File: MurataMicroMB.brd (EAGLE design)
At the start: 90 x 63 mm, 54 parts, among them CON1 C-2395, CON2 WM17143CT-ND, CON3 CON_MIL_10_ARM, CON4 C-2395, IC1 NC7SZ00M5XCT-ND, IC2 296-35164-1-ND, IC3 IC_LPC11U3XQFN33, IC4 AZ1117EH-3.3TRG1DICT-ND, Q1 1253-1168-1-ND, SW1 P-8073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

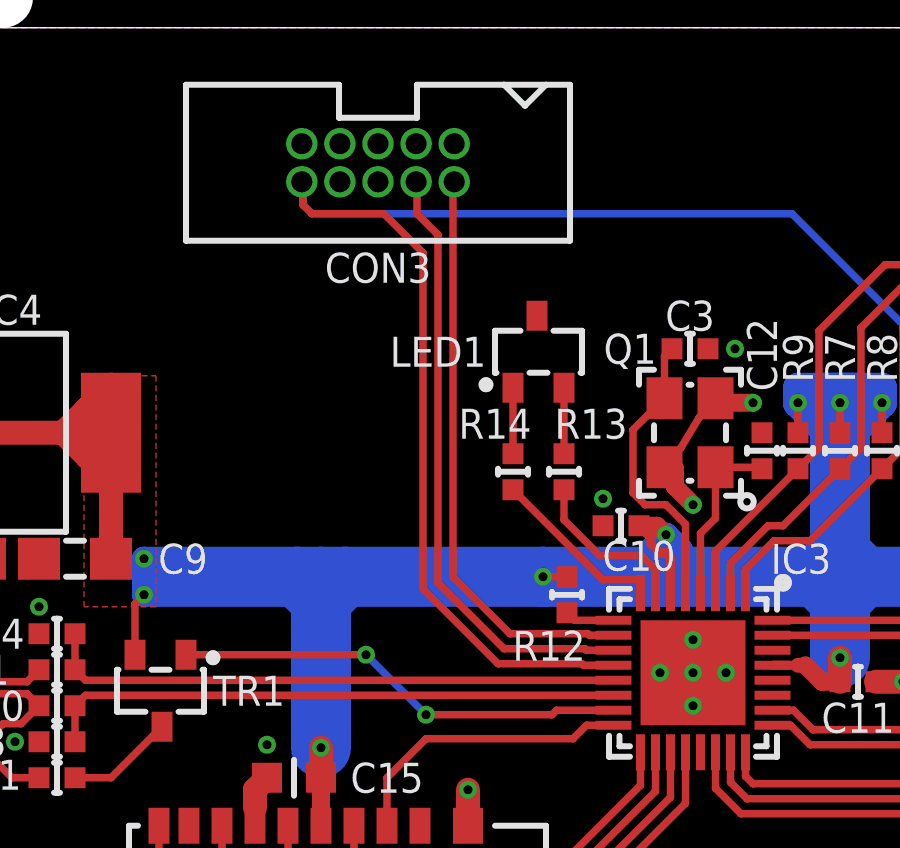
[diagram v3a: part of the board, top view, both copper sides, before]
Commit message: [ MB ] add R17-19
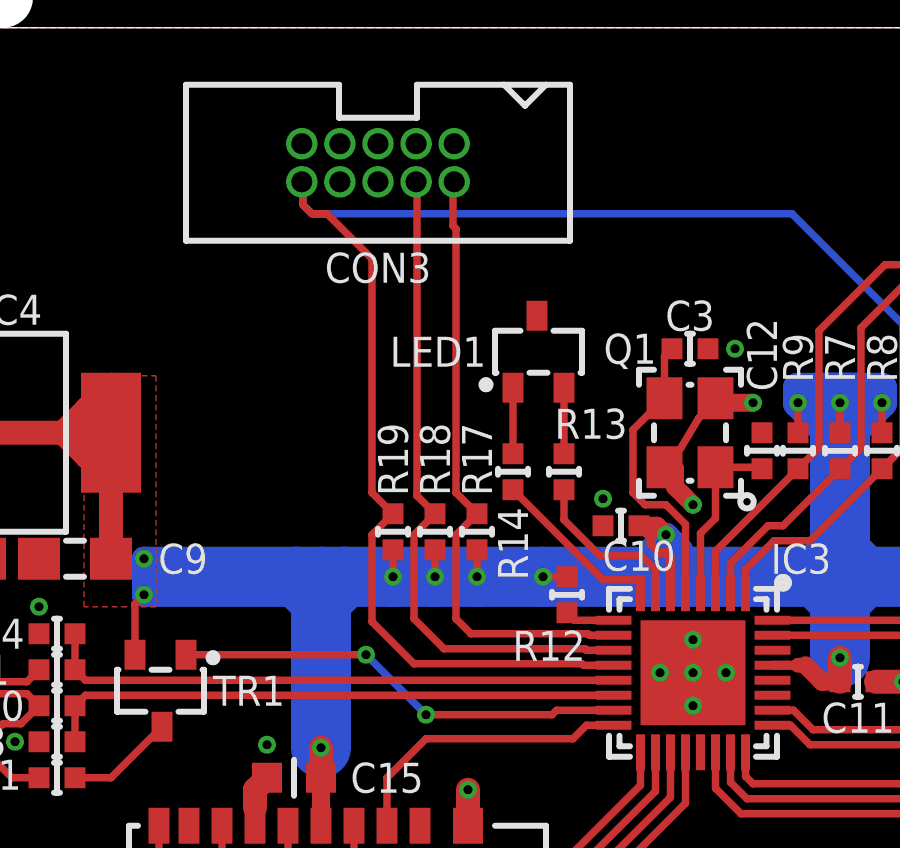
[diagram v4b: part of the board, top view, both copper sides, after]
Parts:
- added R17, R18, R19: 10k/1005, mylib:C0402
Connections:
- net 3.3V: now also R17.2, R18.2, R19.2
- net NSRST: now also R19.1
- net SWCLK: now also R18.1
- net SWDIO: now also R17.1
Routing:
- net 3.3V: track 131.2 -> 133.9 mm, vias 11 -> 14
- net SWCLK: track 20.4 -> 22.2 mm
- net SWDIO: track 19.4 -> 20.7 mm
- net NSRST: track 59.9 -> 61.0 mm
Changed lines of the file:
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@@
 </element>
 <element name="R14" library="mylib" package="C0402" value="100/1005" x="36" y="38.2" smashed="yes" rot="R90">
-<attribute name="NAME" x="35.4" y="39.8" size="1" layer="25" font="vector" ratio="20" rot="R180" align="center"/>
+<attribute name="NAME" x="36" y="35.8" size="1" layer="25" font="vector" ratio="20" rot="R270" align="center"/>
 <attribute name="VALUE" x="37.9" y="37.6" size="1" layer="27" font="vector" ratio="20" rot="R90"/>
 </element>
@@
 <attribute name="MF" value="" x="62.4" y="18.7" size="1.2" layer="27" ratio="17" rot="R180" display="off"/>
 <attribute name="OC_FARNELL" value="unknown" x="62.4" y="18.7" size="1.2" layer="27" ratio="17" rot="R180" display="off"/>
+</element>
+<element name="R17" library="mylib" package="C0402" value="10k/1005" x="34.8" y="36.2" smashed="yes" rot="R270">
+<attribute name="NAME" x="35.3" y="37.4" size="1" layer="25" font="vector" ratio="20" rot="R90"/>
+<attribute name="VALUE" x="32.9" y="36.8" size="1" layer="27" font="vector" ratio="20" rot="R270"/>
+</element>
+<element name="R18" library="mylib" package="C0402" value="10k/1005" x="33.4" y="36.2" smashed="yes" rot="R270">
+<attribute name="NAME" x="33.9" y="37.4" size="1" layer="25" font="vector" ratio="20" rot="R90"/>
+<attribute name="VALUE" x="31.5" y="36.8" size="1" layer="27" font="vector" ratio="20" rot="R270"/>
+</element>
+<element name="R19" library="mylib" package="C0402" value="10k/1005" x="32" y="36.2" smashed="yes" rot="R270">
+<attribute name="NAME" x="32.5" y="37.4" size="1" layer="25" font="vector" ratio="20" rot="R90"/>
+<attribute name="VALUE" x="30.1" y="36.8" size="1" layer="27" font="vector" ratio="20" rot="R270"/>
 </element>
 </elements>
@@
 <wire x1="32.77" y1="47.865" x2="32.77" y2="47.83" width="0.25" layer="1"/>
 <wire x1="32.77" y1="47.83" x2="32.8" y2="47.8" width="0.25" layer="1"/>
-<wire x1="32.8" y1="47.8" x2="32.8" y2="46.8" width="0.25" layer="1"/>
-<wire x1="32.8" y1="46.8" x2="33.5" y2="46.1" width="0.25" layer="1"/>
-<wire x1="33.5" y1="46.1" x2="33.5" y2="34.5" width="0.25" layer="1"/>
-<wire x1="33.5" y1="34.5" x2="35.7" y2="32.3" width="0.25" layer="1"/>
-<wire x1="35.7" y1="32.3" x2="38.4" y2="32.3" width="0.25" layer="1"/>
+<wire x1="32.7" y1="33.3" x2="33.7" y2="32.3" width="0.25" layer="1"/>
+<wire x1="33.7" y1="32.3" x2="38.4" y2="32.3" width="0.25" layer="1"/>
+<wire x1="32.8" y1="47.8" x2="32.8" y2="37.4" width="0.25" layer="1"/>
+<contactref element="R18" pad="1"/>
+<wire x1="32.7" y1="36.1" x2="32.7" y2="33.3" width="0.25" layer="1"/>
+<wire x1="33.4" y1="36.8" x2="32.7" y2="36.1" width="0.25" layer="1"/>
+<wire x1="32.8" y1="37.4" x2="33.4" y2="36.8" width="0.25" layer="1"/>
 </signal>
 <signal name="SWDIO">
@@
 <wire x1="34.1" y1="47.805" x2="34.1" y2="47.8" width="0.25" layer="1"/>
 <wire x1="34.1" y1="47.8" x2="34" y2="47.7" width="0.25" layer="1"/>
-<wire x1="34" y1="47.7" x2="34" y2="34.7" width="0.25" layer="1"/>
-<wire x1="34" y1="34.7" x2="35.9" y2="32.8" width="0.25" layer="1"/>
-<wire x1="35.9" y1="32.8" x2="38.5" y2="32.8" width="0.25" layer="1"/>
+<wire x1="34" y1="47.7" x2="34" y2="46.4" width="0.25" layer="1"/>
+<wire x1="34" y1="46.4" x2="34.1" y2="46.3" width="0.25" layer="1"/>
+<wire x1="34.1" y1="46.3" x2="34.1" y2="37.5" width="0.25" layer="1"/>
+<wire x1="34.1" y1="36.1" x2="34.1" y2="33.3" width="0.25" layer="1"/>
+<wire x1="34.1" y1="33.3" x2="34.6" y2="32.8" width="0.25" layer="1"/>
+<wire x1="34.6" y1="32.8" x2="38.5" y2="32.8" width="0.25" layer="1"/>
+<contactref element="R17" pad="1"/>
+<wire x1="34.8" y1="36.8" x2="34.1" y2="36.1" width="0.25" layer="1"/>
+<wire x1="34.1" y1="37.5" x2="34.8" y2="36.8" width="0.25" layer="1"/>
 </signal>
 <signal name="NSRST">
@@
 <wire x1="39.35" y1="31.75" x2="38.35" y2="31.75" width="0.25" layer="1"/>
 <wire x1="38.35" y1="31.75" x2="38.3" y2="31.8" width="0.25" layer="1"/>
-<wire x1="35.5" y1="31.8" x2="38.3" y2="31.8" width="0.25" layer="1"/>
+<wire x1="32.7" y1="31.8" x2="38.3" y2="31.8" width="0.25" layer="1"/>
 <wire x1="29" y1="47.825" x2="29" y2="47.8" width="0.25" layer="1"/>
 <wire x1="29" y1="47.8" x2="28.9" y2="47.7" width="0.25" layer="1"/>
@@
 <wire x1="29.3" y1="46.8" x2="29" y2="47.1" width="0.25" layer="16"/>
 <wire x1="29" y1="47.825" x2="28.96" y2="47.865" width="0.25" layer="1"/>
-<wire x1="35.5" y1="31.8" x2="33" y2="34.3" width="0.25" layer="1"/>
-<wire x1="33" y1="34.3" x2="33" y2="45.5" width="0.25" layer="1"/>
+<wire x1="32.7" y1="31.8" x2="31.3" y2="33.2" width="0.25" layer="1"/>
+<wire x1="31.3" y1="33.2" x2="31.3" y2="36.1" width="0.25" layer="1"/>
+<wire x1="31.3" y1="37.5" x2="31.3" y2="45.3" width="0.25" layer="1"/>
 <wire x1="29" y1="47.6" x2="29" y2="47.1" width="0.25" layer="1"/>
-<wire x1="33" y1="45.5" x2="31.7" y2="46.8" width="0.25" layer="1"/>
-<wire x1="31.7" y1="46.8" x2="29.3" y2="46.8" width="0.25" layer="1"/>
+<wire x1="31.3" y1="45.3" x2="29.8" y2="46.8" width="0.25" layer="1"/>
+<wire x1="29.8" y1="46.8" x2="29.3" y2="46.8" width="0.25" layer="1"/>
 <wire x1="29.3" y1="46.8" x2="29" y2="47.1" width="0.25" layer="1"/>
+<contactref element="R19" pad="1"/>
+<wire x1="32" y1="36.8" x2="31.3" y2="36.1" width="0.25" layer="1"/>
+<wire x1="31.3" y1="37.5" x2="32" y2="36.8" width="0.25" layer="1"/>
 </signal>
 <signal name="3.3V">
@@
 <wire x1="28.8" y1="34.7" x2="29.6" y2="34.7" width="2" layer="16"/>
 <wire x1="29.6" y1="34.7" x2="30.4" y2="34.7" width="2" layer="16"/>
-<wire x1="30.4" y1="34.7" x2="37" y2="34.7" width="2" layer="16"/>
+<wire x1="30.4" y1="34.7" x2="32" y2="34.7" width="2" layer="16"/>
+<wire x1="32" y1="34.7" x2="33.4" y2="34.7" width="2" layer="16"/>
+<wire x1="33.4" y1="34.7" x2="34.8" y2="34.7" width="2" layer="16"/>
+<wire x1="34.8" y1="34.7" x2="37" y2="34.7" width="2" layer="16"/>
 <wire x1="37" y1="34.7" x2="41.1" y2="34.7" width="2" layer="16"/>
 <wire x1="23.7" y1="35.3" x2="24.4" y2="34.7" width="0.8" layer="16"/>
@@
 <wire x1="44.65" y1="31.75" x2="45.5" y2="31.75" width="0.3" layer="1"/>
 <wire x1="46.9" y1="32" x2="46.9" y2="31.2" width="0.8" layer="1"/>
+<contactref element="R17" pad="2"/>
+<contactref element="R18" pad="2"/>
+<contactref element="R19" pad="2"/>
+<via x="32" y="34.7" extent="1-16" drill="0.3"/>
+<via x="33.4" y="34.7" extent="1-16" drill="0.3"/>
+<via x="34.8" y="34.7" extent="1-16" drill="0.3"/>
+<wire x1="32" y1="35.6" x2="32" y2="34.7" width="0.25" layer="1"/>
+<wire x1="33.4" y1="35.6" x2="33.4" y2="34.7" width="0.25" layer="1"/>
+<wire x1="34.8" y1="35.6" x2="34.8" y2="34.7" width="0.25" layer="1"/>
 </signal>
 <signal name="N$3">

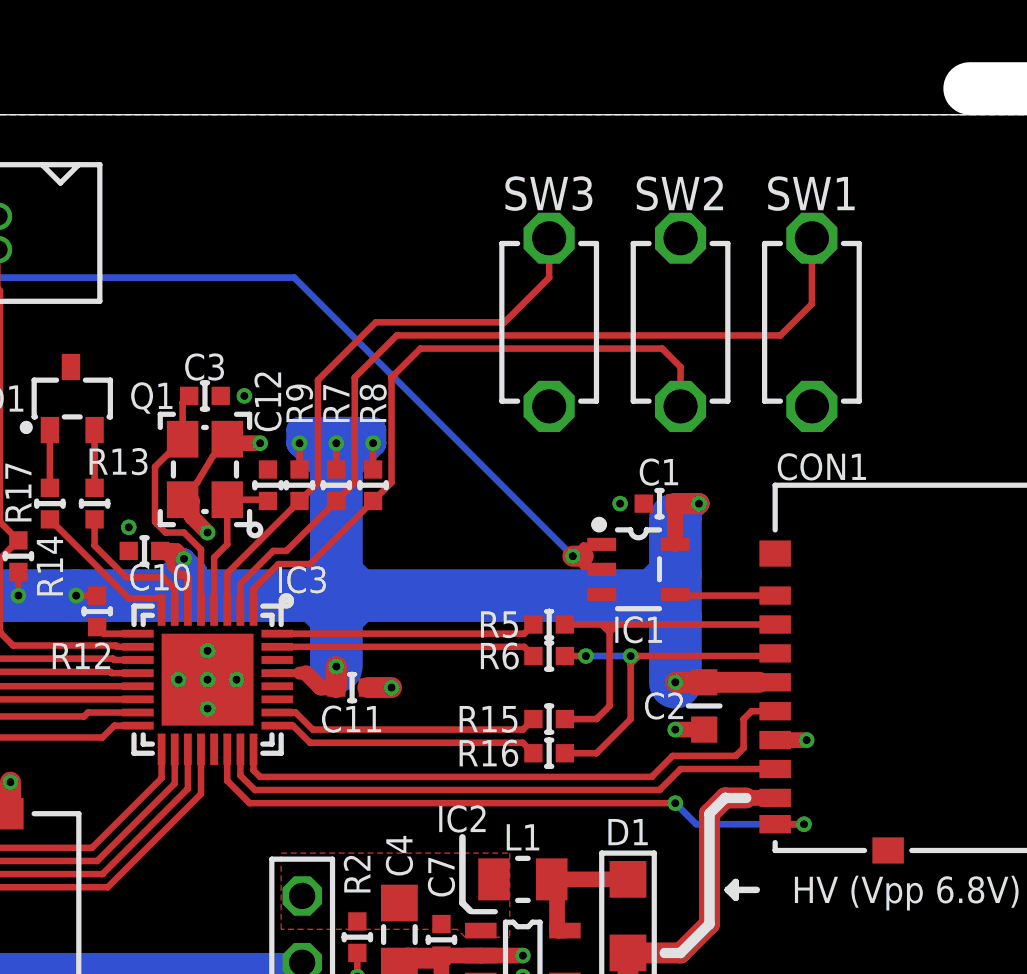
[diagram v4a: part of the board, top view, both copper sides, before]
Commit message: [ MB ] add R20/21; R7/8/9 move
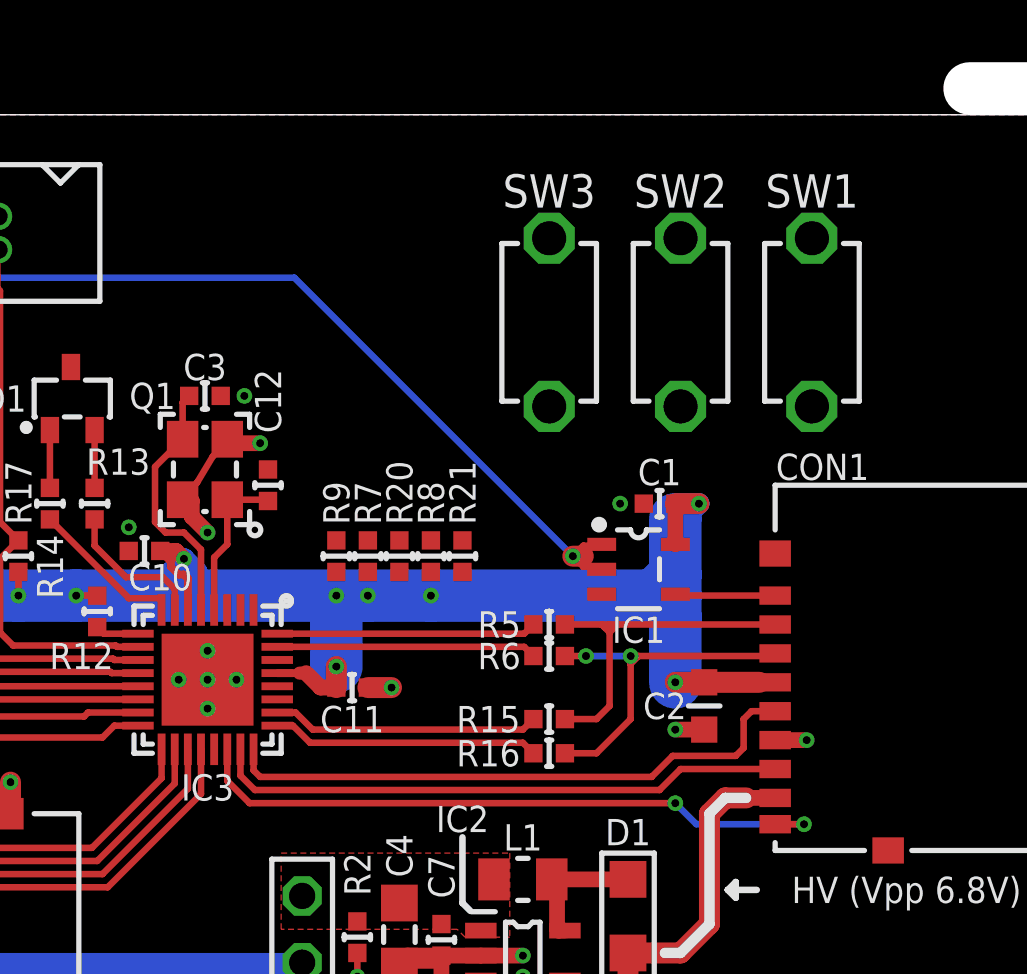
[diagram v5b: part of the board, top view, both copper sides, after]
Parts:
- added R20, R21: 1k/1005, mylib:C0402
- R15, R16, R5, R6: value 33/1005 -> 1k/1005
- moved R8 3.48 mm to (50.5, 36.2), turned to 90 degrees
- moved R9 3.04 mm to (46.9, 36.2), turned to 90 degrees
- moved R7 2.95 mm to (48.1, 36.2), turned to 90 degrees
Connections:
- new net N$19: R21.1, SW2.A2
- new net N$21: IC3.1, R20.2
- net BL: now also R20.1, R21.2; no longer IC3.1, SW2.A2
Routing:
- net !RESET!: track 32.0 -> 0.00 mm
- net 3.3V: track 133.9 -> 108.0 mm
- net BL: track 25.0 -> 0.00 mm
- net ISP: track 22.1 -> 0.00 mm

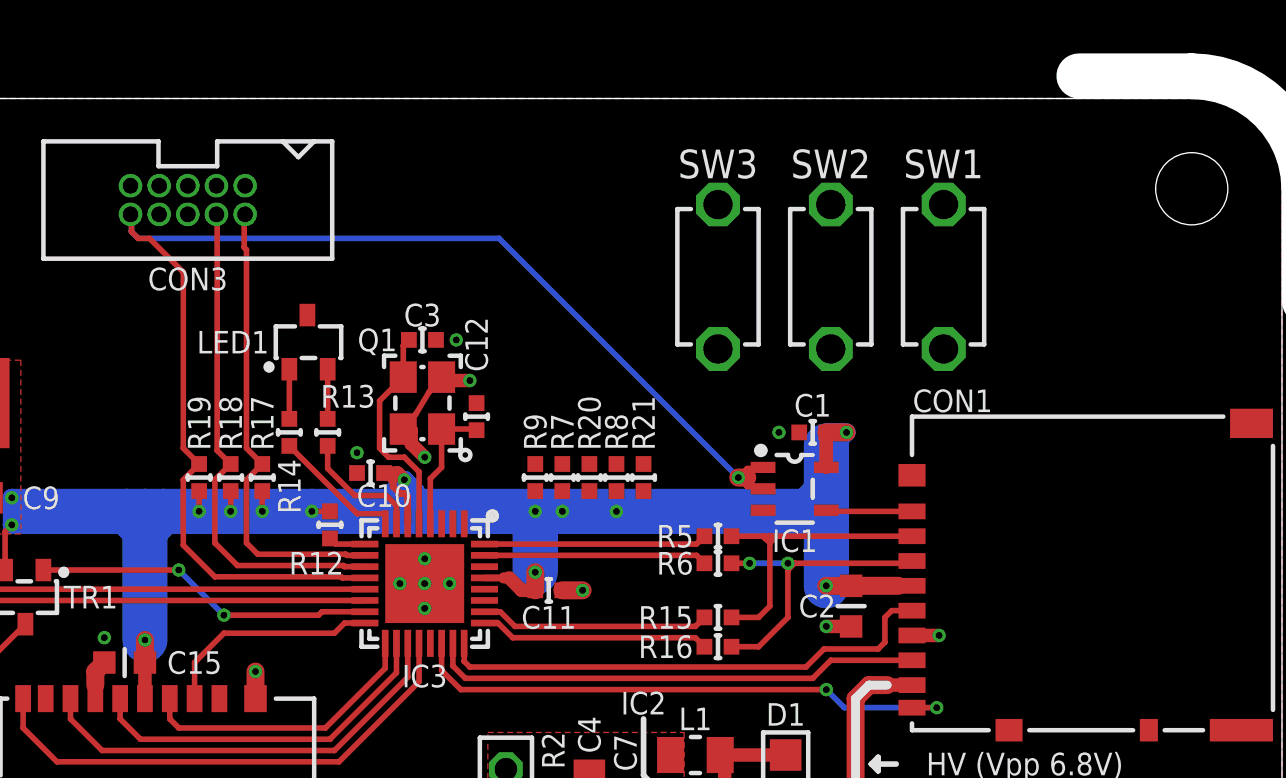
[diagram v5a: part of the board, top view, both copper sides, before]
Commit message: [ MB ] move SW1-3, BL shares IC1 with nSRST
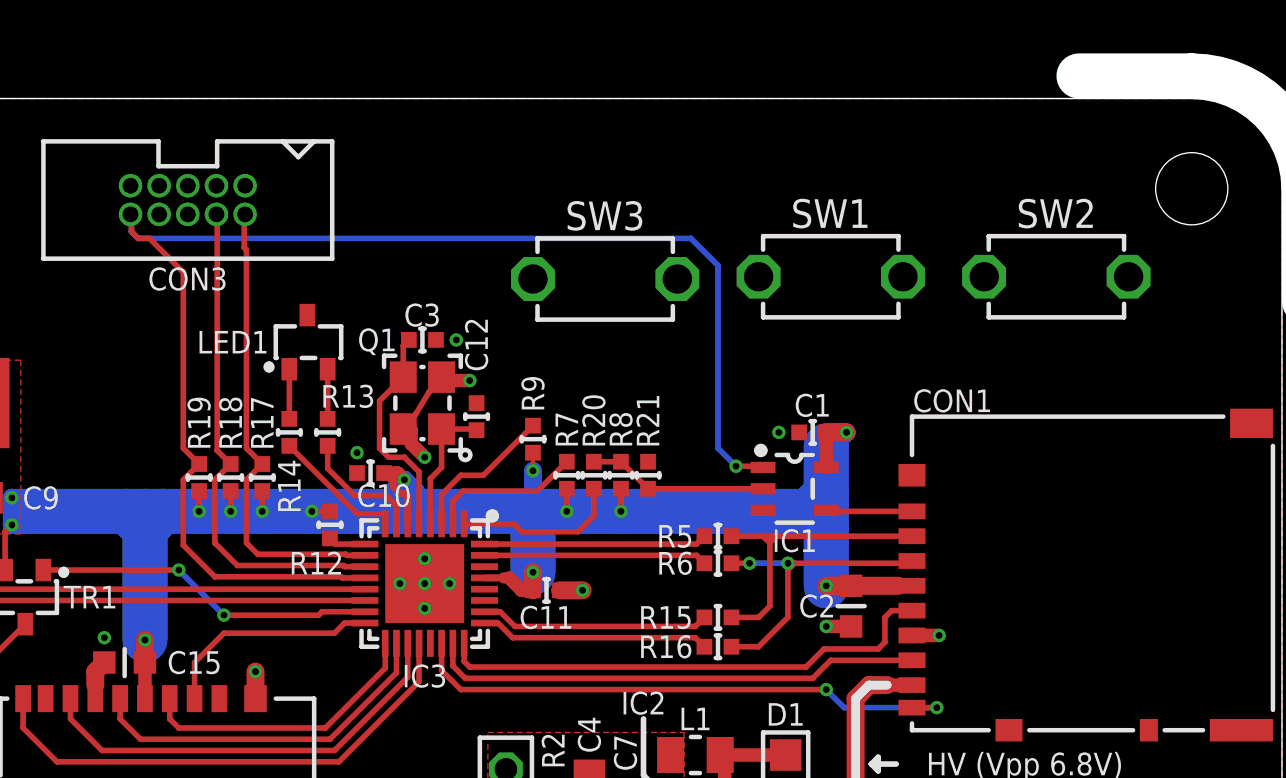
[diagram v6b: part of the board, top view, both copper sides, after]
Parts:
- moved SW2 10.0 mm to (70.0, 45.1), turned to 180 degrees
- moved SW3 5.00 mm to (50.0, 45.0), turned to 180 degrees
- moved SW1 5.00 mm to (60.0, 45.1), turned to 180 degrees
- moved R9 1.70 mm to (46.8, 37.9)
- moved R20 0.22 mm to (49.5, 36.3)
- moved R8 0.22 mm to (50.7, 36.3)
- moved R21 0.22 mm to (51.9, 36.3)
- moved R7 0.22 mm to (48.3, 36.3)
- moved C11 0.10 mm to (47.4, 31.2)
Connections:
- net BL: now also IC1.2
- net NSRST: no longer IC1.2
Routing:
- net BL: track 0.00 -> 8.00 mm
- net N$21: track 0.00 -> 7.38 mm
- net !RESET!: track 0.00 -> 6.77 mm
- net ISP: track 0.00 -> 6.61 mm
- net 3.3V: track 108.0 -> 112.5 mm
- net NSRST: track 61.0 -> 63.2 mm
